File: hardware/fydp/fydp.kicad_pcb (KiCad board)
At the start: 2 copper layers, 8.6 x 6.6 mm, 334 parts, among them J1 1054500101, J10 Conn_01x02_Pin, J11 Conn_01x02_Pin, J12 Conn_01x02_Pin, J13 Conn_01x02_Pin, J14 Conn_01x02_Pin, J15 Conn_01x02_Pin, J16 Conn_01x02_Pin, J17 Conn_01x02_Pin, J18 Conn_01x04_Pin, J2 Conn_01x02_Pin, J23 Conn_01x02_Pin, J24 Conn_01x02_Pin, J25 Conn_01x02_Pin, J26 Conn_01x02_Pin, J27 Conn_01x02_Pin, J3 Conn_01x02_Pin, J4 Conn_01x02_Pin, J5 Conn_01x02_Pin, J6 Conn_01x04_Pin, J7 Conn_01x04_Pin, J8 Conn_01x02_Pin, J9 Conn_01x02_Pin, U1 LTC2630ISC6-LZ8-TRMPBF, U10 SN74LVC1G3157DCKR, U11 AD633ARZ-R7, U12 AD633ARZ-R7, U13 LTC2630ISC6-LZ8-TRMPBF, U14 LTC2630ISC6-LZ8-TRMPBF, U15 SN74LVC1G3157DCKR, U16 SN74LVC1G3157DCKR, U17 AD633ARZ-R7, U18 AD633ARZ-R7, U19 LTC2630ISC6-LZ8-TRMPBF, U2 AD633ARZ-R7, U20 LTC2630ISC6-LZ8-TRMPBF, U21 SN74LVC1G3157DCKR, U22 SN74LVC1G3157DCKR, U23 AD633ARZ-R7, U24 AD633ARZ-R7, U25 LTC2630ISC6-LZ8-TRMPBF, U26 LTC2630ISC6-LZ8-TRMPBF, U27 SN74LVC1G3157DCKR, U28 SN74LVC1G3157DCKR, U29 AD633ARZ-R7, U3 SN74LVC1G3157DCKR, U30 AD633ARZ-R7, U31 LTC2630ISC6-LZ8-TRMPBF, U32 LTC2630ISC6-LZ8-TRMPBF, U33 SN74LVC1G3157DCKR, U34 SN74LVC1G3157DCKR, U35 AD633ARZ-R7, U36 AD633ARZ-R7, U37 LTC2630ISC6-LZ8-TRMPBF, U38 LTC2630ISC6-LZ8-TRMPBF, U39 SN74LVC1G3157DCKR, U4 LTC2630ISC6-LZ8-TRMPBF, U40 SN74LVC1G3157DCKR, U41 AD633ARZ-R7, U42 AD633ARZ-R7, U43 LTC2630ISC6-LZ8-TRMPBF, U44 LTC2630ISC6-LZ8-TRMPBF, U45 SN74LVC1G3157DCKR, U46 SN74LVC1G3157DCKR, U47 AD633ARZ-R7, U48 AD633ARZ-R7, U49 LTC2630ISC6-LZ8-TRMPBF, U5 SN74LVC1G3157DCKR, U50 LTC2630ISC6-LZ8-TRMPBF, U51 LTC2630ISC6-LZ8-TRMPBF, U52 LTC2630ISC6-LZ8-TRMPBF, U53 AD7699BCPZRL7, U54 AD7699BCPZRL7, U55 74HC154D, U56 SN74HC08DR, U57 AD7699BCPZRL7, U58 AD7699BCPZRL7, U59 AZ1117IH-3.3TRG1, U6 AD633ARZ-R7, U60 LM2611BMF/NOPB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

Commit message: Initial layout mostly complete, need to complete lots of routing
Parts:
- removed C100, C111, C112, C117, C118, C123, C124, C135, C136, C141, C142, C147, C148, C159, C160, C165, C166, C171, C172, C183, C184, C189, C190, C206, C207, C208, C210, C211, C212, C214, C215, C216, C218, C219, C220, C237, C240, C63, C64, C69, C70, C75, C76, C87, C88, C93, C94, C99: 0.1uF, Capacitor_SMD:C_0805_2012Metric
- removed C103, C104, C127, C128, C151, C152, C175, C176, C225, C230, C241, C79, C80: 0.01uF, Capacitor_SMD:C_0805_2012Metric
- removed C205, C209, C213, C217: 10uF, Capacitor_SMD:C_0805_2012Metric
- removed C221, C224, C234: 22uF, Capacitor_SMD:C_1206_3216Metric
- removed C222: 10uF, Capacitor_SMD:C_1206_3216Metric
- removed C227, C228, C239: 4.7uF, Capacitor_SMD:C_0805_2012Metric
- removed C231: 2.2uF, Capacitor_SMD:C_1206_3216Metric
- removed the C27 at (88.7, 102.5)
- removed the C28 at (108.7, 102.5)
- removed the J11 at (107.0, 89.5)
- removed the J13 at (107.0, 109.5)
- removed the J16 at (107.0, 129.5)
- removed the J17 at (107.0, 149.5)
- removed the J18 at (68.5, 53.5)
- removed J26, J27: Conn_01x02_Pin, Connector_PinHeader_2.54mm:PinHeader_1x02_P2.54mm_Vertical
- removed the R10 at (76.2, 119.0)
- removed R101, R97: 100, Resistor_SMD:R_0805_2012Metric
- removed the R11 at (56.2, 115.0)
- removed R112: 0, Resistor_SMD:R_0805_2012Metric
- removed the R12 at (76.2, 115.0)
- removed the R13 at (96.2, 119.0)
- removed the R14 at (116.2, 115.0)
- removed the R15 at (96.2, 115.0)
- removed the R16 at (116.2, 119.0)
- removed the R17 at (96.2, 139.0)
- removed the R18 at (116.2, 139.0)
- removed the R19 at (96.2, 135.0)
- removed the R20 at (116.2, 135.0)
- removed the R21 at (56.2, 139.0)
- removed the R26 at (76.2, 159.0)
- removed the R27 at (56.2, 155.0)
- removed the R28 at (76.2, 155.0)
- removed the R29 at (96.2, 159.0)
- removed the R30 at (116.2, 159.0)
- removed the R31 at (96.2, 155.0)
- removed the R32 at (116.2, 155.0)
- removed the R33 at (63.5, 53.5)
- removed the R34 at (64.5, 56.0)
- removed the R35 at (64.5, 58.6)
- removed the R36 at (105.5, 41.0)
- removed the R37 at (40.0, 61.5)
- removed the R38 at (40.0, 59.5)
- removed the R39 at (40.0, 57.5)
- removed the R40 at (64.5, 61.1)
- removed the R5 at (96.2, 99.0)
- removed the R6 at (116.2, 95.0)
- removed the R7 at (96.2, 95.0)
- removed the R8 at (116.2, 99.0)
- removed the R83 at (106.7, 93.5)
- removed the R9 at (56.2, 119.0)
- removed TP30: TestPoint, TestPoint:TestPoint_Pad_1.0x1.0mm
- removed the U10 at (112.7, 98.5)
- removed the U11 at (100.7, 97.0)
- removed the U12 at (120.7, 97.0)
- removed the U13 at (48.7, 118.5)
- removed the U14 at (68.7, 118.5)
- removed the U15 at (52.7, 118.5)
- removed the U21 at (92.7, 118.5)
- removed the U23 at (100.7, 117.0)
- removed the U24 at (120.7, 117.0)
- removed the U26 at (108.7, 138.5)
- removed the U32 at (68.7, 138.5)
- removed the U33 at (112.7, 138.5)
- removed U35, U36, U47, U48: AD633ARZ-R7, fydp:R_8_ADI
- removed U37, U38, U43, U44: LTC2630ISC6-LZ8-TRMPBF, Package_TO_SOT_SMD:SOT-363_SC-70-6_Handsoldering
- removed U45, U46: SN74LVC1G3157DCKR, Package_TO_SOT_SMD:SOT-23-6_Handsoldering
- removed U53, U54, U57, U58: AD7699BCPZRL7, fydp:CP_20_4_ADI
- removed U56: SN74HC08DR, fydp:D14
- removed U63: 74HC14D, fydp:SOT108-1_NEX
- removed the U7 at (88.7, 98.5)
- removed the U8 at (108.7, 98.5)
- removed the U9 at (92.7, 98.5)
- added C1: 4.7uF, Capacitor_SMD:C_0805_2012Metric, F.Cu at (247.4, 85.0)
- added C10: 10uF, Capacitor_SMD:C_0805_2012Metric, F.Cu at (189.8, 71.5)
- added C11: 22uF, Capacitor_SMD:C_0805_2012Metric, F.Cu at (194.3, 77.5)
- added C12: 22uF, Capacitor_SMD:C_0805_2012Metric, F.Cu at (197.3, 77.5)
- added C13: 2.2uF, Capacitor_SMD:C_0805_2012Metric, F.Cu at (196.8, 83.5)
- added C14: 22uF, Capacitor_SMD:C_0805_2012Metric, F.Cu at (202.8, 86.5)
- added C16: 22uF, Capacitor_SMD:C_0805_2012Metric, F.Cu at (191.8, 86.5)
- added C33: 0.1uF, Capacitor_SMD:C_0805_2012Metric, F.Cu at (158.3, 88.5)
- added C34: 0.1uF, Capacitor_SMD:C_0805_2012Metric, F.Cu at (159.3, 100.0)
- added C35: 0.01uF, Capacitor_SMD:C_0805_2012Metric, F.Cu at (170.8, 100.0)
- added C36: 0.1uF, Capacitor_SMD:C_0805_2012Metric, F.Cu at (164.3, 100.0)
- added C37: 0.1uF, Capacitor_SMD:C_0805_2012Metric, F.Cu at (178.3, 88.5)
- added C38: 0.1uF, Capacitor_SMD:C_0805_2012Metric, F.Cu at (179.3, 100.0)
- added C41: 0.1uF, Capacitor_SMD:C_0805_2012Metric, F.Cu at (158.3, 104.5)
- added C42: 0.1uF, Capacitor_SMD:C_0805_2012Metric, F.Cu at (159.3, 116.0)
- added C43: 0.01uF, Capacitor_SMD:C_0805_2012Metric, F.Cu at (170.8, 116.0)
- added C44: 0.1uF, Capacitor_SMD:C_0805_2012Metric, F.Cu at (164.3, 116.0)
- added C47: 0.01uF, Capacitor_SMD:C_0805_2012Metric, F.Cu at (150.8, 132.0)
- added C48: 0.1uF, Capacitor_SMD:C_0805_2012Metric, F.Cu at (144.3, 132.0)
- added C49: 0.1uF, Capacitor_SMD:C_0805_2012Metric, F.Cu at (158.3, 120.5)
- added C5: 4.7uF, Capacitor_SMD:C_0805_2012Metric, F.Cu at (247.4, 97.0)
- added C50: 0.1uF, Capacitor_SMD:C_0805_2012Metric, F.Cu at (159.3, 132.0)
- added C53: 0.1uF, Capacitor_SMD:C_0805_2012Metric, F.Cu at (178.3, 120.5)
- added C54: 0.1uF, Capacitor_SMD:C_0805_2012Metric, F.Cu at (179.3, 132.0)
- added C57: 0.1uF, Capacitor_SMD:C_0805_2012Metric, F.Cu at (188.6, 127.8)
- added C58: 0.1uF, Capacitor_SMD:C_0805_2012Metric, F.Cu at (190.6, 127.8)
- added C59: 0.1uF, Capacitor_SMD:C_0805_2012Metric, F.Cu at (201.6, 120.6)
- added C60: 0.1uF, Capacitor_SMD:C_0805_2012Metric, F.Cu at (192.6, 129.8)
- added C61: 47uF, Capacitor_SMD:C_0805_2012Metric, F.Cu at (194.6, 127.8)
- added J20: Conn_01x07_Pin, Connector_PinHeader_2.54mm:PinHeader_1x07_P2.54mm_Vertical, F.Cu at (212.8, 131.1)
- added J5: Conn_01x02_Pin, Connector_PinHeader_2.54mm:PinHeader_1x02_P2.54mm_Vertical, F.Cu at (185.8, 96.3)
- added J7: Conn_01x02_Pin, Connector_PinHeader_2.54mm:PinHeader_1x02_P2.54mm_Vertical, F.Cu at (188.6, 84.5)
- added R48: 4.7k, Resistor_SMD:R_0805_2012Metric, F.Cu at (136.9, 130.4)
- added R49: 4.7k, Resistor_SMD:R_0805_2012Metric, F.Cu at (136.9, 122.7)
- added R50: 4.7k, Resistor_SMD:R_0805_2012Metric, F.Cu at (139.1, 120.4)
- added R51: 4.7k, Resistor_SMD:R_0805_2012Metric, F.Cu at (139.1, 116.4)
- added R52: 4.7k, Resistor_SMD:R_0805_2012Metric, F.Cu at (108.1, 118.2)
- added R53: 4.7k, Resistor_SMD:R_0805_2012Metric, F.Cu at (108.1, 116.2)
- added R54: 4.7k, Resistor_SMD:R_0805_2012Metric, F.Cu at (108.1, 110.2)
- added R55: 4.7k, Resistor_SMD:R_0805_2012Metric, F.Cu at (136.9, 114.2)
- added R66: 1K, Resistor_SMD:R_0805_2012Metric, F.Cu at (153.3, 96.5)
- added R67: 1K, Resistor_SMD:R_0805_2012Metric, F.Cu at (153.3, 92.5)
- added R68: 1K, Resistor_SMD:R_0805_2012Metric, F.Cu at (173.3, 96.5)
- added R69: 1K, Resistor_SMD:R_0805_2012Metric, F.Cu at (173.3, 92.5)
- added R72: 1K, Resistor_SMD:R_0805_2012Metric, F.Cu at (153.3, 112.5)
- added R73: 1K, Resistor_SMD:R_0805_2012Metric, F.Cu at (153.3, 108.5)
- added R74: 1K, Resistor_SMD:R_0805_2012Metric, F.Cu at (173.3, 112.5)
- added R75: 1K, Resistor_SMD:R_0805_2012Metric, F.Cu at (173.3, 108.5)
- added R78: 1K, Resistor_SMD:R_0805_2012Metric, F.Cu at (153.3, 128.5)
- added R79: 1K, Resistor_SMD:R_0805_2012Metric, F.Cu at (153.3, 124.5)
- added R80: 1K, Resistor_SMD:R_0805_2012Metric, F.Cu at (173.3, 128.5)
- added R81: 1K, Resistor_SMD:R_0805_2012Metric, F.Cu at (173.3, 124.5)
- added R85: 4.7k, Resistor_SMD:R_0805_2012Metric, F.Cu at (186.6, 123.8)
- added R86: 0, Resistor_SMD:R_0805_2012Metric, F.Cu at (190.6, 131.3)
- added R89: 0, Resistor_SMD:R_0805_2012Metric, F.Cu at (196.1, 131.3)
- added R90: 100, Resistor_SMD:R_0805_2012Metric, F.Cu at (208.3, 131.1)
- added R91: 100, Resistor_SMD:R_0805_2012Metric, F.Cu at (208.3, 128.5)
- added R92: 100, Resistor_SMD:R_0805_2012Metric, F.Cu at (208.3, 126.0)
- added TP15: TestPoint, TestPoint:TestPoint_Pad_1.0x1.0mm, F.Cu at (146.8, 97.3)
- added TP16: TestPoint, TestPoint:TestPoint_Pad_1.0x1.0mm, F.Cu at (166.8, 97.3)
- added U17: SN74LVC1G3157DCKR, Package_TO_SOT_SMD:SOT-23-6_Handsoldering, F.Cu at (149.8, 96.0)
- added U28: LTC2630ISC6-LZ8-TRMPBF, Package_TO_SOT_SMD:SOT-363_SC-70-6_Handsoldering, F.Cu at (144.3, 128.0)
- C2, C3, C4, C6: value 0.1uF -> 4.7uF
- C32, C55: value 0.01uF -> 0.1uF
- C39, C51: value 0.1uF -> 0.01uF
- C56: value 0.01uF -> 2.2uF
- C7: renamed from C223; footprint Capacitor_SMD:C_1206_3216Metric -> Capacitor_SMD:C_0805_2012Metric
- C9: renamed from C235; footprint Capacitor_SMD:C_1206_3216Metric -> Capacitor_SMD:C_0805_2012Metric
- R22, R23, R24, R25: value 1K -> 4.7k
- R84: value 100 -> 4.7k
- R87: value 100 -> 1K
- R88: value 100 -> 0
- U16, U22: value SN74LVC1G3157DCKR -> LTC2630ISC6-LZ8-TRMPBF; footprint Package_TO_SOT_SMD:SOT-23-6_Handsoldering -> Package_TO_SOT_SMD:SOT-363_SC-70-6_Handsoldering
- U20: value LTC2630ISC6-LZ8-TRMPBF -> SN74LVC1G3157DCKR; footprint Package_TO_SOT_SMD:SOT-363_SC-70-6_Handsoldering -> Package_TO_SOT_SMD:SOT-23-6_Handsoldering
- U34: value SN74LVC1G3157DCKR -> LTC2353ILX-16-PBF; footprint Package_TO_SOT_SMD:SOT-23-6_Handsoldering -> Package_QFP:LQFP-48_7x7mm_P0.5mm
- moved C6 199.2 mm to (247.4, 100.0), turned to 0 degrees
- moved J11 182.9 mm to (107.7, 138.0), turned to 180 degrees
- moved J12 182.2 mm to (107.7, 126.2), turned to 90 degrees
- moved J13 172.1 mm to (107.7, 122.2), turned to 90 degrees
- moved R29 166.6 mm to (114.1, 130.2), turned to 180 degrees
- moved R30 165.1 mm to (114.1, 128.2), turned to 180 degrees
- moved R32 163.8 mm to (114.1, 126.2), turned to 180 degrees
- moved R33 162.5 mm to (114.1, 124.2), turned to 180 degrees
- moved R36 161.3 mm to (114.1, 122.2), turned to 180 degrees
- moved R44 160.2 mm to (114.1, 120.2), turned to 180 degrees
- moved C2 159.2 mm to (247.4, 88.0), turned to 0 degrees
- moved R38 159.1 mm to (114.1, 118.2), turned to 0 degrees
- moved R40 158.2 mm to (114.1, 116.2), turned to 0 degrees
- moved R42 157.4 mm to (114.1, 114.2), turned to 0 degrees
- moved R1 157.1 mm to (188.3, 106.5), turned to 90 degrees
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- renumbered C232 to C15, C226 to C17, C229 to C18, C194 to C19, C197 to C20, C200 to C21, C203 to C22, C1 to C23, C11 to C24, C5 to C25, C8 to C26, C16 to C27, C14 to C28, C23 to C29, C20 to C30, C233 to C8, D4 to D2, D2 to D4, J3 to J10, J6 to J11, J4 to J12, J5 to J13, J8 to J14, J9 to J15, J10 to J16, J12 to J17, J14 to J18, J15 to J19, J24 to J2, J23 to J3, J25 to J6, J7 to J8, J2 to J9, L2 to L1, L1 to L2, R107 to R1, R76 to R10, R75 to R11, R69 to R12, R70 to R13, R74 to R14, R67 to R15, R73 to R16, R68 to R17, R72 to R18, R42 to R19, R110 to R2, R71 to R20, R44 to R21, R47 to R26, R48 to R27, R49 to R28, R66 to R29, R108 to R3, R65 to R30, R50 to R31, R63 to R32, R64 to R33, R51 to R34, R52 to R35, R45 to R36, R53 to R37, R62 to R38, R54 to R39, R109 to R4, R61 to R40, R55 to R41, R60 to R42, R56 to R43, R46 to R44, R59 to R45, R57 to R46, R58 to R47, R111 to R5, R77 to R56, R78 to R57, R1 to R58, R2 to R59, R105 to R6, R3 to R60, R4 to R61, R79 to R62, R81 to R63, R80 to R64, R82 to R65, R106 to R7, R85 to R70, R86 to R71, R89 to R76, R90 to R77, R41 to R8, R91 to R82, R92 to R83, R43 to R9, U61 to U1, U1 to U10, U3 to U11, U2 to U12, U4 to U13, U5 to U14, U6 to U15, U17 to U18, U59 to U2, U18 to U21, U27 to U23, U29 to U24, U28 to U26, U30 to U27, U39 to U29, U60 to U3, U41 to U30, U40 to U32, U42 to U33, U62 to U4, U55 to U5, U49 to U6, U50 to U7, U51 to U8, U52 to U9
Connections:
- net /ANALOG MULTIPLIER 3/GPIO_SW5_POLARITY_R renamed /ANALOG MULTIPLIER 2/GPIO_SW5_POLARITY_R
- net /ANALOG MULTIPLIER 3/GPIO_SW6_POLARITY_R renamed /ANALOG MULTIPLIER 2/GPIO_SW6_POLARITY_R
- net /ANALOG MULTIPLIER 5/GPIO_SW10_POLARITY renamed /ANALOG MULTIPLIER 3/GPIO_SW10_POLARITY
- net /ANALOG MULTIPLIER 5/GPIO_SW10_POLARITY_R renamed /ANALOG MULTIPLIER 3/GPIO_SW10_POLARITY_R
- net /ANALOG MULTIPLIER 5/GPIO_SW9_POLARITY renamed /ANALOG MULTIPLIER 3/GPIO_SW9_POLARITY
- net /ANALOG MULTIPLIER 5/GPIO_SW9_POLARITY_R renamed /ANALOG MULTIPLIER 3/GPIO_SW9_POLARITY_R
- net /ANALOG MULTIPLIER 5/MULT9_Y1 renamed /ANALOG MULTIPLIER 3/MULT9_Y1
- net /ANALOG MULTIPLIER 7/GPIO_SW13_POLARITY renamed /ANALOG MULTIPLIER 4/GPIO_SW13_POLARITY
- net /ANALOG MULTIPLIER 7/GPIO_SW13_POLARITY_R renamed /ANALOG MULTIPLIER 4/GPIO_SW13_POLARITY_R
- net /ANALOG MULTIPLIER 7/GPIO_SW14_POLARITY renamed /ANALOG MULTIPLIER 4/GPIO_SW14_POLARITY
- net /ANALOG MULTIPLIER 7/GPIO_SW14_POLARITY_R renamed /ANALOG MULTIPLIER 4/GPIO_SW14_POLARITY_R
- net /ANALOG MULTIPLIER 7/MULT13_Y2 renamed /ANALOG MULTIPLIER 4/MULT13_Y2
- net /ANALOG MULTIPLIER 7/MULT14_Y1 renamed /ANALOG MULTIPLIER 4/MULT14_Y1
- net /ANALOG MULTIPLIER 7/MULT14_Y2 renamed /ANALOG MULTIPLIER 4/MULT14_Y2
- net /DAC INPUTS/DAC_IN_CLK renamed DAC_IN_CLK
- net /DAC INPUTS/DAC_IN_DATA_IN renamed DAC_IN_DATA_IN
- net /DECODER 2/DAC_DECODER_A0 renamed DAC_DECODER_A0
- net /DECODER 2/DAC_DECODER_A1 renamed DAC_DECODER_A1
- net /DECODER 2/DAC_DECODER_A2 renamed DAC_DECODER_A2
- net /DECODER 2/DAC_DECODER_A3 renamed DAC_DECODER_A3
- C17 pad 1: /DECODER 1/PP3V3 -> +3.3V
- C18 pad 1: /DECODER 2/PP3V3 -> +3.3V
- C19 pad 1: /DAC INPUTS/PP5V0 -> +5V
- C2 pad 1: /ADC 2/PP5V0 -> +5V
- C20 pad 1: /DAC INPUTS/PP5V0 -> +5V
- C21 pad 1: /DAC INPUTS/PP5V0 -> +5V
- C22 pad 1: /DAC INPUTS/PP5V0 -> +5V
- C23 pad 1: /ANALOG MULTIPLIER 1/PP5V0 -> +5V
- C24 pad 1: /ANALOG MULTIPLIER 1/PP5V0 -> +5V
- C25 pad 1: /ANALOG MULTIPLIER 1/PP15V0 -> +15V
- C26 pad 1: /ANALOG MULTIPLIER 1/PN15V0 -> -15V
- C27 pad 1: /ANALOG MULTIPLIER 1/PP5V0 -> +5V
- C28 pad 1: /ANALOG MULTIPLIER 1/PP5V0 -> +5V
- C29 pad 1: /ANALOG MULTIPLIER 1/PP15V0 -> +15V
- C3 pad 1: /ADC 3/PP5V0 -> +5V
- C30 pad 1: /ANALOG MULTIPLIER 1/PN15V0 -> -15V
- C31 pad 1: /ANALOG MULTIPLIER 2/PP5V0 -> +5V
- C32 pad 1: /ANALOG MULTIPLIER 2/PP5V0 -> +5V
- C39 pad 1: /ANALOG MULTIPLIER 2/PN15V0 -> +5V
- C4 pad 1: /ADC 4/PP5V0 -> +5V
- C40 pad 1: /ANALOG MULTIPLIER 2/PN15V0 -> +5V
- C45 pad 1: /ANALOG MULTIPLIER 2/PP15V0 -> +15V
- C46 pad 1: /ANALOG MULTIPLIER 2/PP15V0 -> -15V
- C51 pad 1: /ANALOG MULTIPLIER 3/PP5V0 -> +5V
- C52 pad 1: /ANALOG MULTIPLIER 3/PP5V0 -> +5V
- C55 pad 1: /ANALOG MULTIPLIER 3/PP5V0 -> +5V
- C56 pad 1: /ANALOG MULTIPLIER 3/PP5V0 -> /ADC/ADC1_VDDLBYP
- C6 pad 1: /ADC 1/PP5V0 -> +5V
- C7 pad 2: /POWER/PP5V0 -> +5V
- C9 pad 1: /POWER/PP15V0 -> /POWER/PP15V0_BOOST
- D1 pad 1: /USBC RECEPTACLE/PP5V0 -> +5V
- D2 pad 1: /USBC RECEPTACLE/PP5V0 -> +5V
- J10 pad 1: /DECODER 1/PP3V3 -> +3.3V
- J12 pad 1: /DECODER 2/PP3V3 -> +3.3V
- J13 pad 1: /DECODER 2/PP3V3 -> +3.3V
- J2 pad 2: /USBC RECEPTACLE/PP5V0 -> +5V
- J3 pad 2: /USBC RECEPTACLE/PP5V0 -> +5V
- J6 pad 2: /POWER/PP3V3 -> +3.3V
- J9 pad 1: /DECODER 1/PP3V3 -> +3.3V
- L1 pad 1: /POWER/PP5V0 -> +5V
- L2 pad 1: /POWER/PP5V0 -> +5V
- R15 pad 2: ADC1_CS_L -> /DECODER 1/TP_ADC1_CS_L
- R17 pad 2: ADC2_CS_L -> /DECODER 1/TP_ADC2_CS_L
- R19 pad 2: ADC3_CS_L -> /DECODER 1/TP_ADC3_CS_L
- R2 pad 1: /POWER/PP5V0 -> +5V
- R21 pad 2: ADC4_CS_L -> /DECODER 1/TP_ADC4_CS_L
- R22 pad 1: /ANALOG MULTIPLIER 5/MULT10_Y1 -> /DECODER 1/TP_ADC1_CS_L
- R23 pad 1: /ANALOG MULTIPLIER 5/MULT9_Y2 -> /DECODER 1/TP_ADC2_CS_L
- R24 pad 1: /ANALOG MULTIPLIER 5/MULT10_Y2 -> /DECODER 1/TP_ADC3_CS_L
- R25 pad 1: /ANALOG MULTIPLIER 7/MULT13_Y1 -> /DECODER 1/TP_ADC4_CS_L
- R26 pad 2: /DECODER 2/DAC1_CS_L -> DAC1_CS_L
- R27 pad 2: /DECODER 2/DAC2_CS_L -> DAC2_CS_L
- R34 pad 2: /DECODER 2/DAC5_CS_L -> DAC5_CS_L
- R35 pad 2: /DECODER 2/DAC6_CS_L -> DAC6_CS_L
- R41 pad 2: /DECODER 2/DAC9_CS_L -> DAC9_CS_L
- R42 pad 1: /DECODER 2/DAC14_CS_L -> DAC14_CS_L
- R43 pad 2: /DECODER 2/DAC10_CS_L -> DAC10_CS_L
- R45 pad 1: /DECODER 2/DAC13_CS_L -> DAC13_CS_L
- R5 pad 1: /POWER/PP5V0 -> +5V
- R62 pad 1: /ANALOG MULTIPLIER 1/DAC_CLK -> DAC_CLK
- R64 pad 1: /ANALOG MULTIPLIER 1/DAC_DATA_IN -> DAC_DATA_IN
- R70 pad 1: /ANALOG MULTIPLIER 3/GPIO_SW5_POLARITY -> /ANALOG MULTIPLIER 2/GPIO_SW5_POLARITY
- R71 pad 1: /ANALOG MULTIPLIER 3/GPIO_SW6_POLARITY -> /ANALOG MULTIPLIER 2/GPIO_SW6_POLARITY
- R84 pad 1: /ANALOG MULTIPLIER 2/GPIO_SW4_POLARITY -> Net-(U34-IN1)
- R84 pad 2: /ANALOG MULTIPLIER 2/GPIO_SW4_POLARITY_R -> GND
- R87 pad 1: /ANALOG MULTIPLIER 4/GPIO_SW7_POLARITY -> /ADC/ADC1_POWER_DOWN
- R87 pad 2: /ANALOG MULTIPLIER 4/GPIO_SW7_POLARITY_R -> GND
- R88 pad 1: /ANALOG MULTIPLIER 4/GPIO_SW8_POLARITY -> Net-(U34-LVDS/*CMOS)
- R88 pad 2: /ANALOG MULTIPLIER 4/GPIO_SW8_POLARITY_R -> GND
- R93 pad 1: /ANALOG MULTIPLIER 6/GPIO_SW11_POLARITY -> ADC1_SDO_CH0
- R93 pad 2: /ANALOG MULTIPLIER 6/GPIO_SW11_POLARITY_R -> /ADC/ADC1_SDO_CH0_R
- R94 pad 1: /ANALOG MULTIPLIER 6/GPIO_SW12_POLARITY -> ADC1_SDO_CH1
- R94 pad 2: /ANALOG MULTIPLIER 6/GPIO_SW12_POLARITY_R -> /ADC/ADC1_SDO_CH1_R
- R95 pad 1: /ANALOG MULTIPLIER 8/GPIO_SW15_POLARITY -> TP_ADC1_CLK_OUT
- R95 pad 2: /ANALOG MULTIPLIER 8/GPIO_SW15_POLARITY_R -> /ADC/TP_ADC1_CLK_OUT_R
- R96 pad 1: /ANALOG MULTIPLIER 8/GPIO_SW16_POLARITY -> ADC1_BUSY_OUT
- R96 pad 2: /ANALOG MULTIPLIER 8/GPIO_SW16_POLARITY_R -> /ADC/ADC1_BUSY_OUT_R
- TP1 pad 1: /ADC 1/TP_ADC1_IN7 -> /DECODER 1/TP_ADC1_CS_L
- TP10 pad 1: /ADC 2/TP_ADC2_IN5 -> /DECODER 2/DAC15_CS_L
- TP11 pad 1: /ADC 2/TP_ADC2_IN4 -> /DECODER 2/DAC8_CS_L
- TP12 pad 1: /ADC 2/TP_ADC2_IN3 -> /DECODER 2/DAC16_CS_L
- TP13 pad 1: /ADC 2/TP_ADC2_IN2 -> /ANALOG MULTIPLIER 1/DAC1_VOUT
- TP14 pad 1: /ADC 2/TP_ADC2_IN1 -> /ANALOG MULTIPLIER 1/DAC2_VOUT
- TP17 pad 1: /ADC 3/TP_ADC3_IN7 -> /ANALOG MULTIPLIER 3/DAC9_VOUT
- TP18 pad 1: /ADC 3/TP_ADC3_IN6 -> /ANALOG MULTIPLIER 3/DAC10_VOUT
- TP19 pad 1: /ADC 3/TP_ADC3_IN5 -> /ANALOG MULTIPLIER 4/DAC13_VOUT
- TP2 pad 1: /ADC 1/TP_ADC1_IN6 -> /DECODER 1/TP_ADC2_CS_L
- TP20 pad 1: /ADC 3/TP_ADC3_IN4 -> /ANALOG MULTIPLIER 4/DAC14_VOUT
- TP21 pad 1: /ADC 3/TP_ADC3_IN3 -> Net-(U34-IN1)
- TP22 pad 1: /ADC 3/TP_ADC3_IN2 -> Net-(U34-IN0)
- TP23 pad 1: /ADC 3/TP_ADC3_IN1 -> /ADC/ADC1_EXTERNAL_REFIN
- TP24 pad 1: /ADC 4/TP_ADC4_IN7 -> /ADC/ADC1_EXTERN_REF
- TP25 pad 1: /ADC 4/TP_ADC4_IN6 -> /ADC/TP_ADC1_SDO_N
- TP26 pad 1: /ADC 4/TP_ADC4_IN5 -> TP_ADC1_CLK_OUT
- TP27 pad 1: /ADC 4/TP_ADC4_IN4 -> /ADC/TP_ADC1_SDO_P
- TP28 pad 1: /ADC 4/TP_ADC4_IN3 -> /ADC/TP_ADC1_SDI_N
- TP29 pad 1: /ADC 4/TP_ADC4_IN2 -> /ADC/TP_ADC1_SDI_P
- TP3 pad 1: /ADC 1/TP_ADC1_IN5 -> /DECODER 1/TP_ADC3_CS_L
- TP4 pad 1: /ADC 1/TP_ADC1_IN4 -> /DECODER 1/TP_ADC4_CS_L
- TP5 pad 1: /ADC 1/TP_ADC1_IN3 -> /DECODER 2/DAC3_CS_L
- TP6 pad 1: /ADC 1/TP_ADC1_IN2 -> /DECODER 2/DAC11_CS_L
- TP7 pad 1: /ADC 1/TP_ADC1_IN1 -> /DECODER 2/DAC4_CS_L
- TP8 pad 1: /ADC 2/TP_ADC2_IN7 -> /DECODER 2/DAC12_CS_L
- TP9 pad 1: /ADC 2/TP_ADC2_IN6 -> /DECODER 2/DAC7_CS_L
- U1 pad 5: /POWER/PP5V0 -> +5V
- U10 pad 1: /ANALOG MULTIPLIER 1/DAC1_CS_L -> DAC1_CS_L
- U10 pad 2: /ANALOG MULTIPLIER 1/DAC_CLK -> DAC_CLK
- U10 pad 3: /ANALOG MULTIPLIER 1/DAC_DATA_IN -> DAC_DATA_IN
- U10 pad 4: /ANALOG MULTIPLIER 1/PP5V0 -> +5V
- U11 pad 5: /ANALOG MULTIPLIER 1/PP5V0 -> +5V
- U12 pad 3: /ANALOG MULTIPLIER 1/PN15V0 -> -15V
- U12 pad 5: /ANALOG MULTIPLIER 1/MULT1_OUT -> MULT1_OUT
- U12 pad 6: /ANALOG MULTIPLIER 1/PP15V0 -> +15V
- U12 pad 7: /ANALOG MULTIPLIER 1/IN1 -> IN1
- U13 pad 1: /ANALOG MULTIPLIER 1/DAC2_CS_L -> DAC2_CS_L
- U13 pad 2: /ANALOG MULTIPLIER 1/DAC_CLK -> DAC_CLK
- U13 pad 3: /ANALOG MULTIPLIER 1/DAC_DATA_IN -> DAC_DATA_IN
- U13 pad 4: /ANALOG MULTIPLIER 1/PP5V0 -> +5V
- U14 pad 5: /ANALOG MULTIPLIER 1/PP5V0 -> +5V
- U15 pad 3: /ANALOG MULTIPLIER 1/PN15V0 -> -15V
- U15 pad 5: /ANALOG MULTIPLIER 1/MULT2_OUT -> MULT2_OUT
- U15 pad 6: /ANALOG MULTIPLIER 1/PP15V0 -> +15V
- U15 pad 7: /ANALOG MULTIPLIER 1/IN1 -> IN1
- U16 pad 1: /ANALOG MULTIPLIER 3/MULT6_Y1 -> DAC5_CS_L
- U16 pad 2: GND -> DAC_CLK
- U16 pad 3: /ANALOG MULTIPLIER 3/MULT6_Y2 -> DAC_DATA_IN
- U16 pad 4: /ANALOG MULTIPLIER 3/DAC6_VOUT -> +5V
- U16 pad 5: /ANALOG MULTIPLIER 3/PP5V0 -> GND
- U16 pad 6: /ANALOG MULTIPLIER 3/GPIO_SW6_POLARITY -> /ANALOG MULTIPLIER 2/DAC5_VOUT
- U18 pad 1: /ANALOG MULTIPLIER 3/MULT5_Y1 -> /ANALOG MULTIPLIER 2/MULT5_Y1
- U18 pad 2: /ANALOG MULTIPLIER 3/MULT5_Y2 -> /ANALOG MULTIPLIER 2/MULT5_Y2
- U18 pad 3: /ANALOG MULTIPLIER 3/PN15V0 -> -15V
- U18 pad 4: /ANALOG MULTIPLIER 3/MULT1_OUT -> MULT1_OUT
- U18 pad 5: /ANALOG MULTIPLIER 3/MULT5_OUT -> MULT5_OUT
- U18 pad 6: /ANALOG MULTIPLIER 3/PP15V0 -> +15V
- U18 pad 7: /ANALOG MULTIPLIER 3/IN2 -> IN2
- U19 pad 1: /ANALOG MULTIPLIER 4/DAC7_CS_L -> DAC6_CS_L
- U19 pad 2: /ANALOG MULTIPLIER 4/DAC_CLK -> DAC_CLK
- U19 pad 3: /ANALOG MULTIPLIER 4/DAC_DATA_IN -> DAC_DATA_IN
- U19 pad 4: /ANALOG MULTIPLIER 4/PP5V0 -> +5V
- U19 pad 6: /ANALOG MULTIPLIER 4/DAC7_VOUT -> /ANALOG MULTIPLIER 2/DAC6_VOUT
- U2 pad 3: /POWER/PP5V0 -> +5V
- U20 pad 1: /ANALOG MULTIPLIER 4/DAC8_CS_L -> /ANALOG MULTIPLIER 2/MULT6_Y1
- U20 pad 2: /ANALOG MULTIPLIER 4/DAC_CLK -> GND
- U20 pad 3: /ANALOG MULTIPLIER 4/DAC_DATA_IN -> /ANALOG MULTIPLIER 2/MULT6_Y2
- U20 pad 4: /ANALOG MULTIPLIER 4/PP5V0 -> /ANALOG MULTIPLIER 2/DAC6_VOUT
- U20 pad 5: GND -> +5V
- U20 pad 6: /ANALOG MULTIPLIER 4/DAC8_VOUT -> /ANALOG MULTIPLIER 2/GPIO_SW6_POLARITY
- U21 pad 1: /ANALOG MULTIPLIER 3/MULT6_Y1 -> /ANALOG MULTIPLIER 2/MULT6_Y1
- U21 pad 2: /ANALOG MULTIPLIER 3/MULT6_Y2 -> /ANALOG MULTIPLIER 2/MULT6_Y2
- U21 pad 3: /ANALOG MULTIPLIER 3/PN15V0 -> -15V
- U21 pad 4: /ANALOG MULTIPLIER 3/MULT2_OUT -> MULT2_OUT
- U21 pad 5: /ANALOG MULTIPLIER 3/MULT6_OUT -> MULT6_OUT
- U21 pad 6: /ANALOG MULTIPLIER 3/PP15V0 -> +15V
- U21 pad 7: /ANALOG MULTIPLIER 3/IN2 -> IN2
- U22 pad 1: /ANALOG MULTIPLIER 4/MULT8_Y1 -> DAC9_CS_L
- U22 pad 2: GND -> DAC_CLK
- U22 pad 3: /ANALOG MULTIPLIER 4/MULT8_Y2 -> DAC_DATA_IN
- U22 pad 4: /ANALOG MULTIPLIER 4/DAC8_VOUT -> +5V
- U22 pad 5: /ANALOG MULTIPLIER 4/PP5V0 -> GND
- U22 pad 6: /ANALOG MULTIPLIER 4/GPIO_SW8_POLARITY -> /ANALOG MULTIPLIER 3/DAC9_VOUT
- U23 pad 3: /ANALOG MULTIPLIER 5/MULT9_Y2 -> /ANALOG MULTIPLIER 3/MULT9_Y2
- U23 pad 4: /ANALOG MULTIPLIER 5/DAC9_VOUT -> /ANALOG MULTIPLIER 3/DAC9_VOUT
- U23 pad 5: /ANALOG MULTIPLIER 5/PP5V0 -> +5V
- U24 pad 2: /ANALOG MULTIPLIER 5/MULT9_Y2 -> /ANALOG MULTIPLIER 3/MULT9_Y2
- U24 pad 3: /ANALOG MULTIPLIER 5/PN15V0 -> -15V
- U24 pad 4: /ANALOG MULTIPLIER 5/MULT5_OUT -> MULT5_OUT
- U24 pad 5: /ANALOG MULTIPLIER 5/MULT9_OUT -> MULT9_OUT
- U24 pad 6: /ANALOG MULTIPLIER 5/PP15V0 -> +15V
- U24 pad 7: /ANALOG MULTIPLIER 5/IN3 -> IN3
- U25 pad 1: /ANALOG MULTIPLIER 6/DAC11_CS_L -> DAC10_CS_L
- U25 pad 2: /ANALOG MULTIPLIER 6/DAC_CLK -> DAC_CLK
- U25 pad 3: /ANALOG MULTIPLIER 6/DAC_DATA_IN -> DAC_DATA_IN
- U25 pad 4: /ANALOG MULTIPLIER 6/PP5V0 -> +5V
- U25 pad 6: /ANALOG MULTIPLIER 6/DAC11_VOUT -> /ANALOG MULTIPLIER 3/DAC10_VOUT
- U26 pad 1: /ANALOG MULTIPLIER 5/MULT10_Y1 -> /ANALOG MULTIPLIER 3/MULT10_Y1
- U26 pad 3: /ANALOG MULTIPLIER 5/MULT10_Y2 -> /ANALOG MULTIPLIER 3/MULT10_Y2
- U26 pad 4: /ANALOG MULTIPLIER 5/DAC10_VOUT -> /ANALOG MULTIPLIER 3/DAC10_VOUT
- U26 pad 5: /ANALOG MULTIPLIER 5/PP5V0 -> +5V
- U27 pad 1: /ANALOG MULTIPLIER 5/MULT10_Y1 -> /ANALOG MULTIPLIER 3/MULT10_Y1
- U27 pad 2: /ANALOG MULTIPLIER 5/MULT10_Y2 -> /ANALOG MULTIPLIER 3/MULT10_Y2
- U27 pad 3: /ANALOG MULTIPLIER 5/PN15V0 -> -15V
- U27 pad 4: /ANALOG MULTIPLIER 5/MULT6_OUT -> MULT6_OUT
- U27 pad 5: /ANALOG MULTIPLIER 5/MULT10_OUT -> MULT10_OUT
- U27 pad 6: /ANALOG MULTIPLIER 5/PP15V0 -> +15V
- U27 pad 7: /ANALOG MULTIPLIER 5/IN3 -> IN3
- U29 pad 1: /ANALOG MULTIPLIER 7/MULT13_Y1 -> /ANALOG MULTIPLIER 4/MULT13_Y1
- U29 pad 4: /ANALOG MULTIPLIER 7/DAC13_VOUT -> /ANALOG MULTIPLIER 4/DAC13_VOUT
- U29 pad 5: /ANALOG MULTIPLIER 7/PP5V0 -> +5V
- U3 pad 5: /POWER/PP5V0 -> +5V
- U30 pad 1: /ANALOG MULTIPLIER 7/MULT13_Y1 -> /ANALOG MULTIPLIER 4/MULT13_Y1
- U30 pad 3: /ANALOG MULTIPLIER 7/PN15V0 -> -15V
- U30 pad 4: /ANALOG MULTIPLIER 7/MULT9_OUT -> MULT9_OUT
- U30 pad 5: /ANALOG MULTIPLIER 7/MULT13_OUT -> MULT13_OUT
- U30 pad 6: /ANALOG MULTIPLIER 7/PP15V0 -> +15V
- U30 pad 7: /ANALOG MULTIPLIER 7/IN4 -> IN4
- U31 pad 1: /ANALOG MULTIPLIER 5/DAC9_CS_L -> DAC14_CS_L
- U31 pad 2: /ANALOG MULTIPLIER 5/DAC_CLK -> DAC_CLK
- U31 pad 3: /ANALOG MULTIPLIER 5/DAC_DATA_IN -> DAC_DATA_IN
- U31 pad 4: /ANALOG MULTIPLIER 5/PP5V0 -> +5V
- U31 pad 6: /ANALOG MULTIPLIER 5/DAC9_VOUT -> /ANALOG MULTIPLIER 4/DAC14_VOUT
- U32 pad 4: /ANALOG MULTIPLIER 7/DAC14_VOUT -> /ANALOG MULTIPLIER 4/DAC14_VOUT
- U32 pad 5: /ANALOG MULTIPLIER 7/PP5V0 -> +5V
- U33 pad 3: /ANALOG MULTIPLIER 7/PN15V0 -> -15V
- U33 pad 4: /ANALOG MULTIPLIER 7/MULT10_OUT -> MULT10_OUT
- U33 pad 5: /ANALOG MULTIPLIER 7/MULT14_OUT -> MULT14_OUT
- U33 pad 6: /ANALOG MULTIPLIER 7/PP15V0 -> +15V
- U33 pad 7: /ANALOG MULTIPLIER 7/IN4 -> IN4
- U34 pad 1: /ANALOG MULTIPLIER 6/MULT12_Y1 -> GND
- U34 pad 3: /ANALOG MULTIPLIER 6/MULT12_Y2 -> Net-(U34-IN1)
- U34 pad 4: /ANALOG MULTIPLIER 6/DAC12_VOUT -> MULT13_OUT
- U34 pad 5: /ANALOG MULTIPLIER 6/PP5V0 -> GND
- U34 pad 6: /ANALOG MULTIPLIER 6/GPIO_SW12_POLARITY -> GND
- U4 pad 16: /DECODER 1/PP3V3 -> +3.3V
- U5 pad 24: /DECODER 2/PP3V3 -> +3.3V
- U6 pad 1: /DAC INPUTS/DAC_IN1_CS_L -> DAC_IN1_CS_L
- U6 pad 4: /DAC INPUTS/PP5V0 -> +5V
- U6 pad 6: /DAC INPUTS/IN1 -> IN1
- U7 pad 1: /DAC INPUTS/DAC_IN2_CS_L -> DAC_IN2_CS_L
- U7 pad 4: /DAC INPUTS/PP5V0 -> +5V
- U7 pad 6: /DAC INPUTS/IN2 -> IN2
- U8 pad 1: /DAC INPUTS/DAC_IN3_CS_L -> DAC_IN3_CS_L
- U8 pad 4: /DAC INPUTS/PP5V0 -> +5V
- U8 pad 6: /DAC INPUTS/IN3 -> IN3
- U9 pad 1: /DAC INPUTS/DAC_IN4_CS_L -> DAC_IN4_CS_L
- U9 pad 4: /DAC INPUTS/PP5V0 -> +5V
- U9 pad 6: /DAC INPUTS/IN4 -> IN4
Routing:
- net DAC_DATA_IN: track 0.00 -> 110.5 mm, vias 0 -> 8
- net DAC_CLK: track 0.00 -> 109.4 mm, vias 0 -> 8
- net DAC_IN_DATA_IN: track 0.00 -> 61.4 mm
- net DAC_IN_CLK: track 0.00 -> 61.0 mm
- net +5V: track 0.00 -> 58.6 mm
- net IN4: track 0.00 -> 43.7 mm
- net IN3: track 0.00 -> 43.7 mm
- net IN2: track 0.00 -> 43.7 mm
- net IN1: track 0.00 -> 43.7 mm
- net /ANALOG MULTIPLIER 3/GPIO_SW9_POLARITY: track 0.00 -> 36.4 mm
- net /ANALOG MULTIPLIER 4/GPIO_SW13_POLARITY: track 0.00 -> 36.4 mm
- net /ANALOG MULTIPLIER 2/GPIO_SW5_POLARITY: track 0.00 -> 36.4 mm
- net /ANALOG MULTIPLIER 1/GPIO_SW1_POLARITY: track 0.00 -> 29.3 mm
- net -15V: track 0.00 -> 28.6 mm
- net +15V: track 0.00 -> 26.6 mm
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- added copper zone on F.Cu, net +5V
- added copper zone on F.Cu, net /POWER/BOOST1_LX
- added copper zone on B.Cu, net GND
- added copper zone on F.Cu, net GND
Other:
- board size 8.6 x 6.6 mm -> 104 x 64 mm
- rule pad_to_mask_clearance: 0 -> 0.038

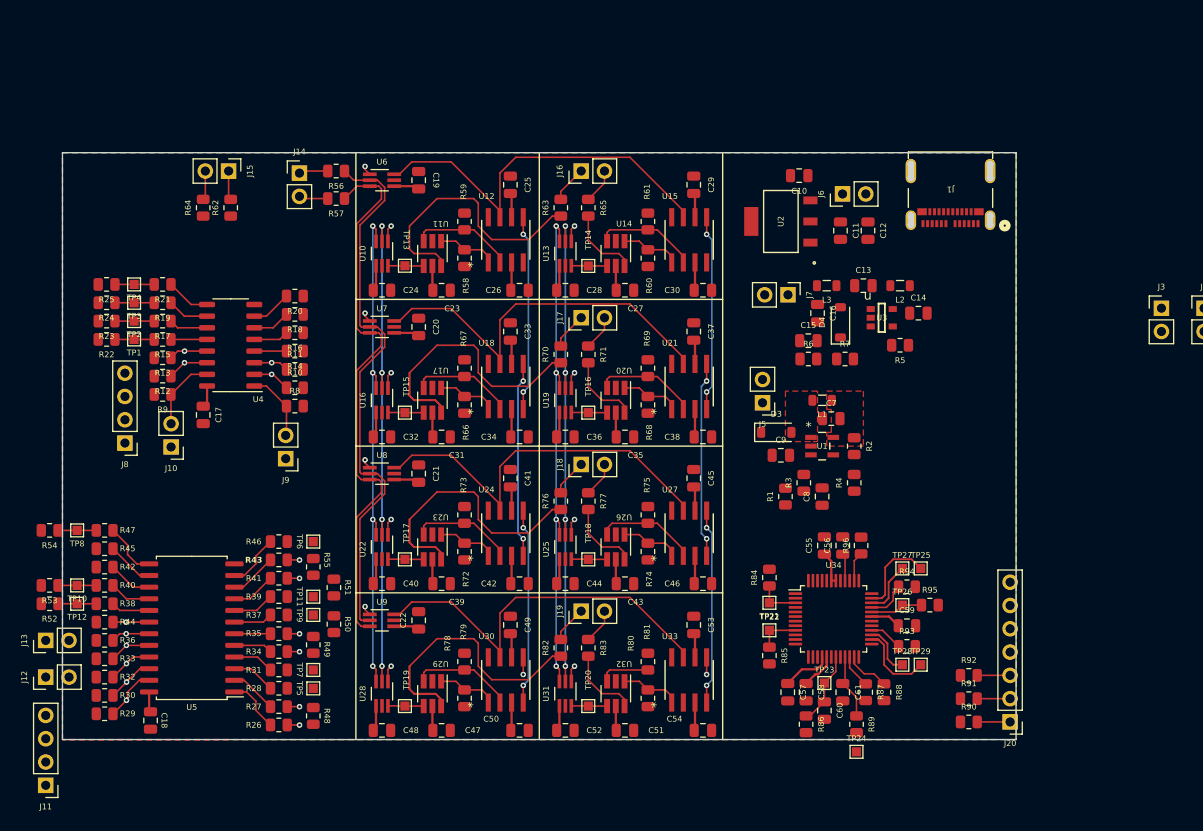
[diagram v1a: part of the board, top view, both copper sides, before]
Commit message: Completed placement and silk for left and centre sections of the PCB
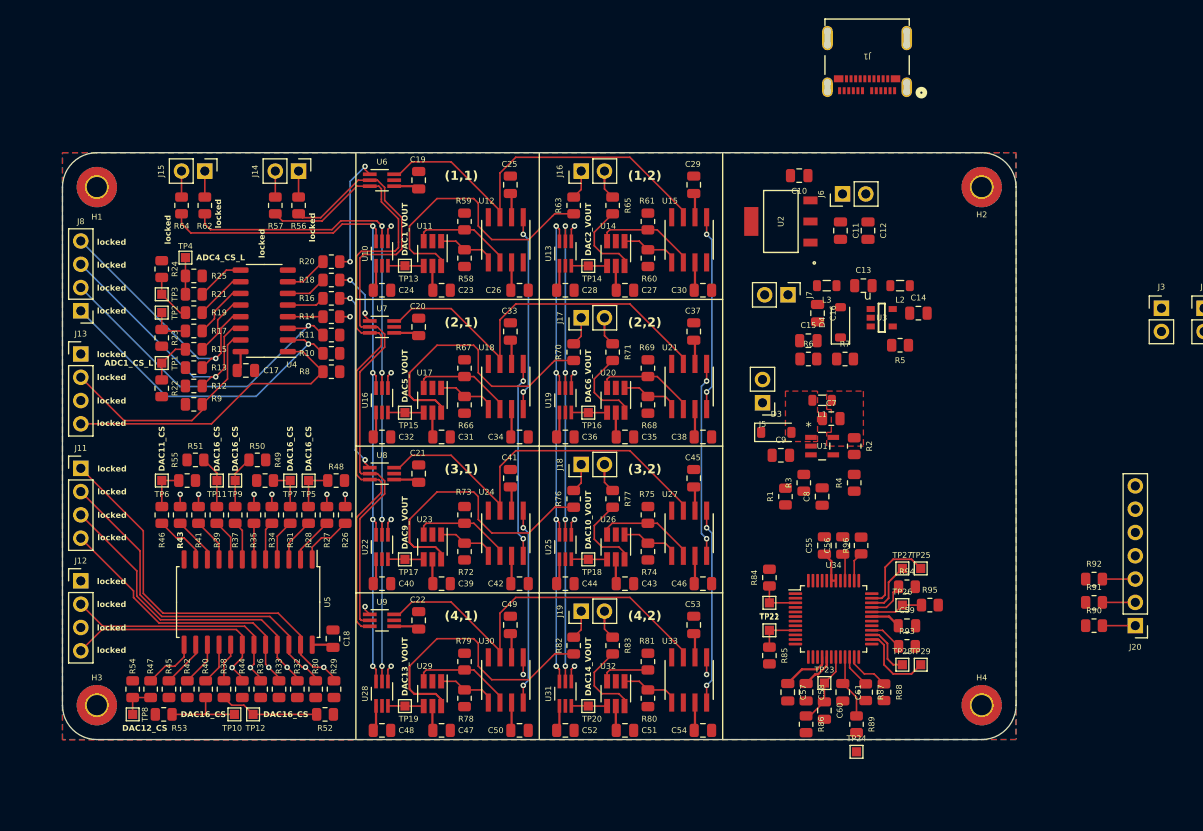
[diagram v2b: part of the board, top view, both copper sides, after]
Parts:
- removed J10, J9: Conn_01x02_Pin, Connector_PinHeader_2.54mm:PinHeader_1x02_P2.54mm_Vertical
- added H1: MountingHole_Pad, MountingHole:MountingHole_2.2mm_M2_Pad_TopBottom, F.Cu at (113.2, 72.8)
- added H2: MountingHole_Pad, MountingHole:MountingHole_2.2mm_M2_Pad_TopBottom, F.Cu at (209.8, 72.8)
- added H3: MountingHole_Pad, MountingHole:MountingHole_2.2mm_M2_Pad_TopBottom, F.Cu at (113.2, 129.2)
- added H4: MountingHole_Pad, MountingHole:MountingHole_2.2mm_M2_Pad_TopBottom, F.Cu at (209.8, 129.2)
- J12, J13: value Conn_01x02_Pin -> Conn_01x04_Pin; footprint Connector_PinHeader_2.54mm:PinHeader_1x02_P2.54mm_Vertical -> Connector_PinHeader_2.54mm:PinHeader_1x04_P2.54mm_Vertical
- moved J11 34.8 mm to (111.5, 103.4), turned to 0 degrees
- moved R52 32.4 mm to (138.1, 130.3), turned to 0 degrees
- moved J13 31.5 mm to (111.5, 91.0), turned to 0 degrees
- moved R48 25.8 mm to (139.3, 104.8), turned to 0 degrees
- moved R29 25.2 mm to (139.1, 127.5), turned to -90 degrees
- moved R26 24.0 mm to (140.3, 108.5), turned to 90 degrees
- moved R30 23.0 mm to (137.1, 127.5), turned to -90 degrees
- moved TP5 22.7 mm to (136.3, 104.8), turned to -90 degrees
- moved TP12 22.7 mm to (130.3, 130.3), turned to -90 degrees
- moved TP10 22.2 mm to (128.2, 130.3), turned to -90 degrees
- moved C18 21.8 mm to (139.0, 122.0), turned to 90 degrees
- moved R27 21.5 mm to (138.3, 108.5), turned to 90 degrees
- moved R32 21.1 mm to (135.1, 127.5), turned to -90 degrees
- moved TP8 21.0 mm to (117.2, 130.3), turned to -90 degrees
- moved TP7 20.8 mm to (134.3, 104.8), turned to -90 degrees
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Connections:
- J13 pad 2: /DECODER 2/DAC_DECODER_E0_L -> /DECODER 1/ADC_DECODER_EN_L
- R14 pad 1: DAC_IN1_CS_L -> DAC_IN4_CS_L
- R14 pad 2: /DECODER 1/DAC_IN1_CS_L_R -> /DECODER 1/DAC_IN4_CS_L_R
- R16 pad 1: DAC_IN2_CS_L -> DAC_IN3_CS_L
- R16 pad 2: /DECODER 1/DAC_IN2_CS_L_R -> /DECODER 1/DAC_IN3_CS_L_R
- R18 pad 1: DAC_IN3_CS_L -> DAC_IN2_CS_L
- R18 pad 2: /DECODER 1/DAC_IN3_CS_L_R -> /DECODER 1/DAC_IN2_CS_L_R
- R20 pad 1: DAC_IN4_CS_L -> DAC_IN1_CS_L
- R20 pad 2: /DECODER 1/DAC_IN4_CS_L_R -> /DECODER 1/DAC_IN1_CS_L_R
- U4 pad 4: /DECODER 1/DAC_IN1_CS_L_R -> /DECODER 1/DAC_IN4_CS_L_R
- U4 pad 5: /DECODER 1/DAC_IN2_CS_L_R -> /DECODER 1/DAC_IN3_CS_L_R
- U4 pad 6: /DECODER 1/DAC_IN3_CS_L_R -> /DECODER 1/DAC_IN2_CS_L_R
- U4 pad 7: /DECODER 1/DAC_IN4_CS_L_R -> /DECODER 1/DAC_IN1_CS_L_R
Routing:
- net DAC_DECODER_A0: track 5.90 -> 42.6 mm
- net DAC_DECODER_A1: track 5.15 -> 38.7 mm
- net /DECODER 1/DAC_IN_DECODER_A1: track 3.81 -> 36.4 mm
- net /DECODER 1/DAC_IN_DECODER_A0: track 4.12 -> 35.5 mm
- net DAC_DECODER_A2: track 4.84 -> 34.3 mm
- net DAC_DECODER_A3: track 4.54 -> 30.5 mm
- net /DECODER 1/DAC_IN_DECODER_EN_L: track 7.65 -> 33.5 mm
- net /DECODER 1/ADC_DECODER_A0: track 4.54 -> 28.6 mm
- net /DECODER 1/ADC_DECODER_A1: track 4.24 -> 28.1 mm
- net DAC_DATA_IN: track 110.5 -> 133.4 mm
- net /DECODER 2/DAC_DECODER_E1_L: track 4.24 -> 25.9 mm
- net DAC_CLK: track 109.4 -> 130.7 mm
- net /DECODER 2/DAC_DECODER_E0_L: track 3.94 -> 24.7 mm
- net DAC_IN3_CS_L: track 1.06 -> 20.5 mm, vias 1 -> 2
- net /DECODER 1/ADC_DECODER_EN_L: track 8.04 -> 25.6 mm
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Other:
- outline, holes or cut-outs redrawn
- board text added: "(1,1)"
- board text added: "(1,2)"
- board text added: "(2,1)"
- board text added: "(2,2)"
- board text added: "(3,1)"
- board text added: "(3,2)"
- board text added: "(4,1)"
- board text added: "(4,2)"
- board text added: "ADC1_CS_L"
- board text added: "ADC4_CS_L"
- board text added: "DAC10_VOUT"
- board text added: "DAC11_CS"
- board text added: "DAC12_CS"
- board text added: "DAC13_VOUT"
- board text added: "DAC14_VOUT"
- board text added: "DAC16_CS"
- board text added: "DAC1_VOUT"
- board text added: "DAC2_VOUT"
- board text added: "DAC5_VOUT"
- board text added: "DAC6_VOUT"
- board text added: "DAC9_VOUT"
- board text added: "locked"

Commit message: Pushing all changes, I'm late for class
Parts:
- moved TP24 5.12 mm to (199.8, 130.8)
- moved R89 1.08 mm to (197.0, 130.8), turned to 0 degrees
- moved R86 1.03 mm to (189.8, 130.8), turned to 180 degrees
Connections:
- net Net-(U34-IN0) renamed /ADC/IN0
- net Net-(U34-IN1) renamed /ADC/IN1
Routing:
- net /ADC/ADC1_EXTERNAL_REFIN: track 8.04 -> 8.57 mm
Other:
- board text added: "ADC1_CLK_OUT"
- board text added: "ADC1_SD0_N"
- board text added: "ADC1_SD0_P"
- board text added: "ADC1_SDI_N"
- board text added: "ADC1_SDI_P"
- board text added: "IN0"
- board text added: "IN1"

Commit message: Did some work in class lol
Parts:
- removed J13: Conn_01x04_Pin, Connector_PinHeader_2.54mm:PinHeader_1x04_P2.54mm_Vertical
- J8: value Conn_01x04_Pin -> Conn_01x08_Pin; footprint Connector_PinHeader_2.54mm:PinHeader_1x04_P2.54mm_Vertical -> Connector_PinHeader_2.54mm:PinHeader_1x08_P2.54mm_Vertical
- moved R90 16.6 mm to (205.6, 123.0)
- moved R91 16.6 mm to (205.6, 120.5)
- moved R92 16.6 mm to (205.6, 118.0)
- moved J20 15.2 mm to (211.5, 123.0)
- moved J8 7.62 mm to (111.5, 78.6), turned to 0 degrees
- moved J1 5.51 mm to (200.8, 62.8)
- moved TP23 4.14 mm to (190.5, 130.4)
- moved C60 3.14 mm to (190.5, 127.5)
- moved R89 2.77 mm to (194.2, 130.4)
- moved TP24 2.77 mm to (197.0, 130.4)
- moved C55 2.12 mm to (190.5, 111.5)
- moved C56 2.12 mm to (192.5, 111.5)
- moved C57 2.12 mm to (186.5, 127.5)
- moved C58 2.12 mm to (188.5, 127.5)
- moved C59 2.12 mm to (199.5, 120.2)
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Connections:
- J8 pad 1: /DECODER 1/DAC_IN_DECODER_A0 -> /DECODER 1/ADC_DECODER_A1
- J8 pad 2: /DECODER 1/DAC_IN_DECODER_A1 -> /DECODER 1/ADC_DECODER_A0
- J8 pad 3: /DECODER 1/ADC_DECODER_A0 -> /DECODER 1/DAC_IN_DECODER_A1
- J8 pad 4: /DECODER 1/ADC_DECODER_A1 -> /DECODER 1/DAC_IN_DECODER_A0
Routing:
- net ADC1_CS_L: track 0.00 -> 21.2 mm
- net /ADC/ADC1_SDO_CH0_R: track 0.00 -> 19.4 mm
- net /ADC/ADC1_BUSY_OUT_R: track 0.00 -> 18.2 mm
- net /ADC/TP_ADC1_CLK_OUT_R: track 0.00 -> 15.6 mm
- net ADC1_SDI: track 0.00 -> 13.6 mm, vias 0 -> 2
- net /ADC/ADC1_SDO_CH1_R: track 0.00 -> 12.4 mm
- net MULT14_OUT: track 1.87 -> 12.3 mm, vias 1 -> 0
- net ADC1_SCLK: track 0.00 -> 10.0 mm
- net /ADC/ADC1_EXTERN_REF: track 0.00 -> 1.84 mm
- net /ADC/ADC1_SDI_R: track 3.59 -> 5.00 mm
- net /ADC/ADC1_SCLK_R: track 3.59 -> 5.00 mm
- net /ADC/ADC1_CS_L_R: track 3.59 -> 5.00 mm
- net /ADC/ADC1_EXTERNAL_REFIN: track 8.57 -> 9.89 mm
- net /DECODER 1/DAC_IN_DECODER_EN_L: track 33.5 -> 34.4 mm
- net /DECODER 1/ADC_DECODER_EN_L: track 25.6 -> 26.5 mm
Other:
- board text added: "ADC1_CS"
- board text added: "ADC2_CS"
- board text added: "ADC3_CS"
- board text added: "ADC4_CS"
- board text added: "CLK_OUT"
- board text added: "EXT_REF"
- board text added: "EXT_REF_IN"
- board text added: "SD0_N"
- board text added: "SD0_P"
- board text added: "SDI_N"
- board text added: "SDI_P"
- board text removed: "ADC1_CLK_OUT"
- board text removed: "ADC1_CS_L"
- board text removed: "ADC1_SD0_N"
- board text removed: "ADC1_SD0_P"
- board text removed: "ADC1_SDI_N"
- board text removed: "ADC1_SDI_P"
- board text removed: "ADC4_CS_L"
